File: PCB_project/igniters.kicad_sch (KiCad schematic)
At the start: 27 parts, among them J10 Conn_01x02, J11 Conn_01x02, J12 Conn_01x02, Q12 AO3400A, Q2 AO3401A, Q4 AO3401A, Q6 AO3400A, Q7 AO3400A, Q8 AO3401A

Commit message: Schematic updated
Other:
- title: KP-PTR -> KP-PTR project - PTR_mini
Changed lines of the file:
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@@
 	(paper "A4")
 	(title_block
-		(title "KP-PTR")
-		(date "2023-12-10")
-		(rev "1.1")
+		(title "KP-PTR project - PTR_mini")
+		(date "2026-09-17")
+		(rev "1.0")
 		(company "Polskie Towarzystwo Rakietowe")
 		(comment 1 "bartekM, FlyingBanana, Kretu, Red Labs, Stachu M, U.S. air force i inni")

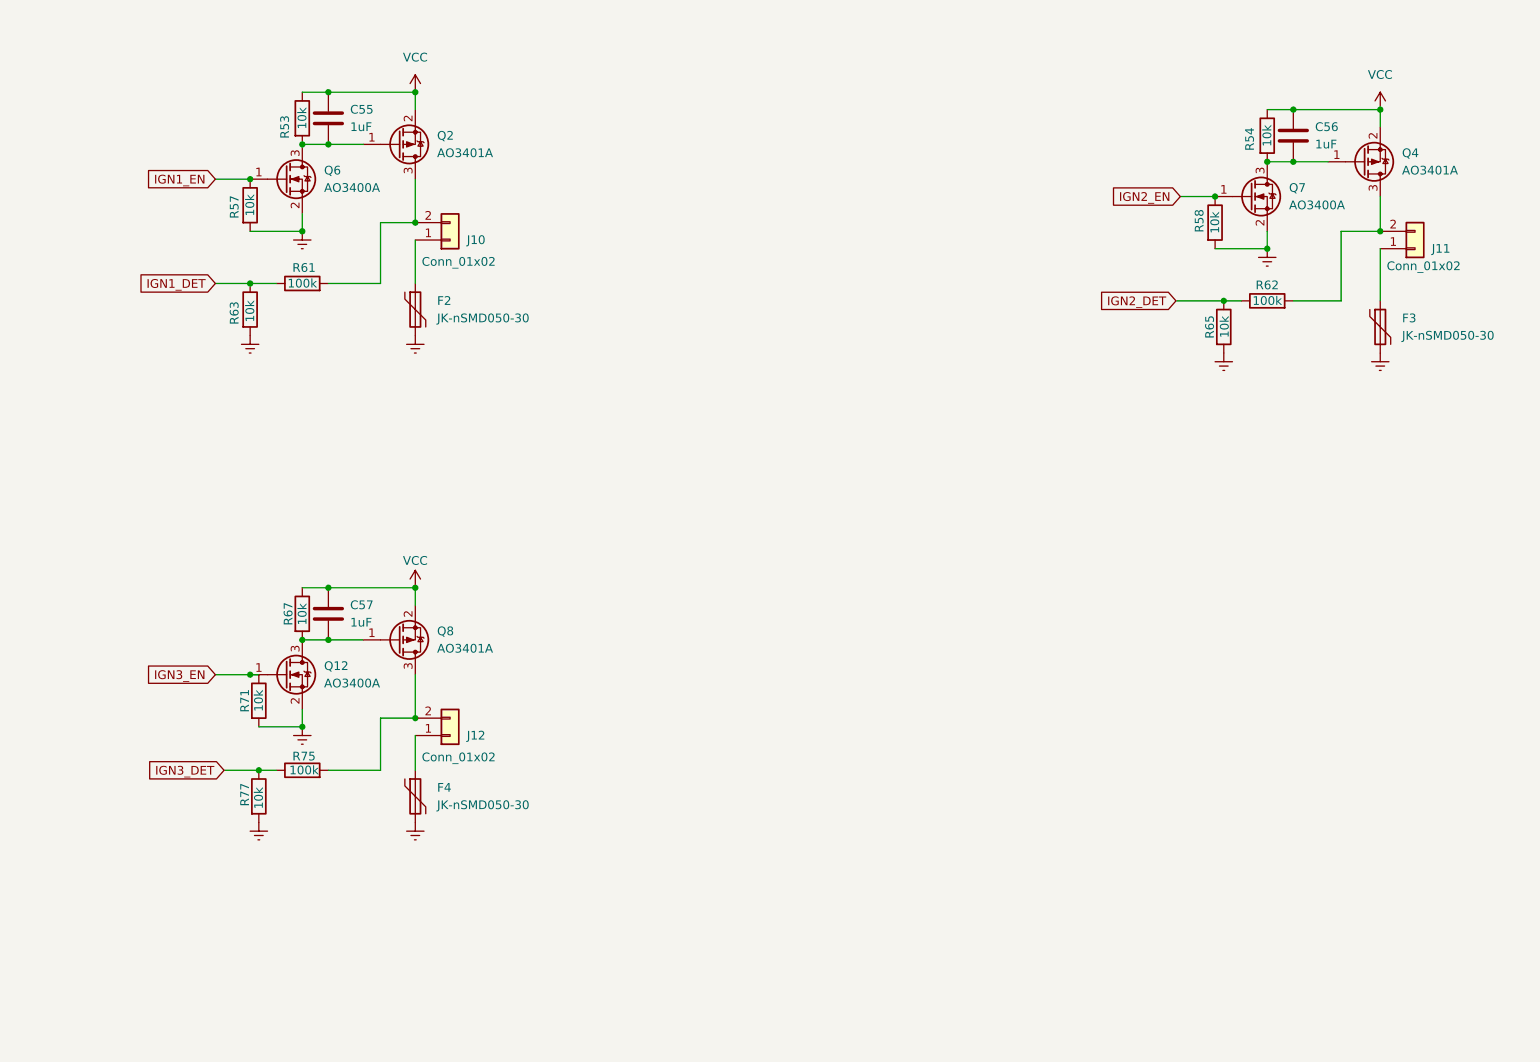
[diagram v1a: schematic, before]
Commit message: + USB connector changed to SMD
+ igniters connectors changed to single 6 pin connector
+ buzzer selected
+ crystal changed to TCXO (experimental)
+ JLC production files generated
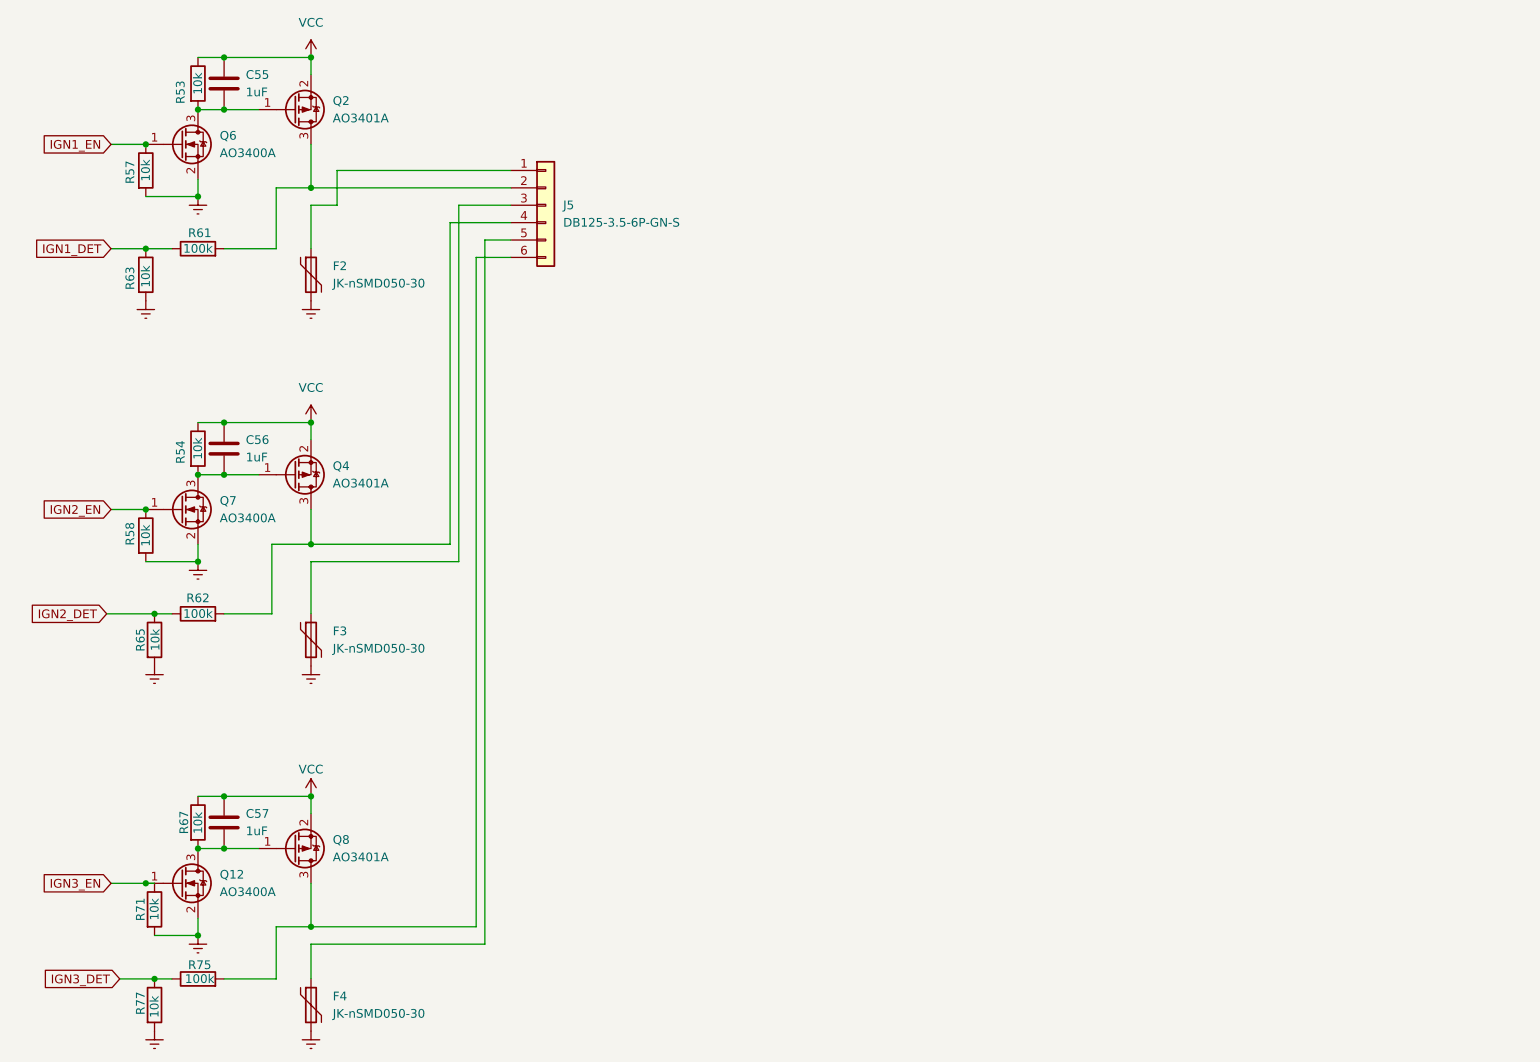
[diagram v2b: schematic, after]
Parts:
- removed J10, J11, J12: Conn_01x02, TerminalBlock_4Ucon:TerminalBlock_4Ucon_1x02_P3.50mm_Horizontal, symbol Connector_Generic:Conn_01x02
- added J5: DB125-3.5-6P-GN-S, TerminalBlock_Phoenix:TerminalBlock_Phoenix_PT-1,5-6-3.5-H_1x06_P3.50mm_Horizontal, symbol Connector_Generic:Conn_01x06
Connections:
- net at F4.1: now also J5.5 (Pin_5)
- net at Q8.3 (D), R75.2: now also J5.6 (Pin_6)
- net at Q2.3 (D), R61.2: now also J5.2 (Pin_2)
- net at Q4.3 (D), R62.2: now also J5.4 (Pin_4)
- net at F3.1: now also J5.3 (Pin_3)
- net at F2.1: now also J5.1 (Pin_1)
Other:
- moved on the sheet: C55, C56, C57, F2, F3, F4, Q12, Q2, Q4, Q6, Q7, Q8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
